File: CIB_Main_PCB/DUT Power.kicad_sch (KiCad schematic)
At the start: 27 parts, among them K18 PC357, K19 PC357, U1 HMSR_30-SMS, U2 HMSR_30-SMS

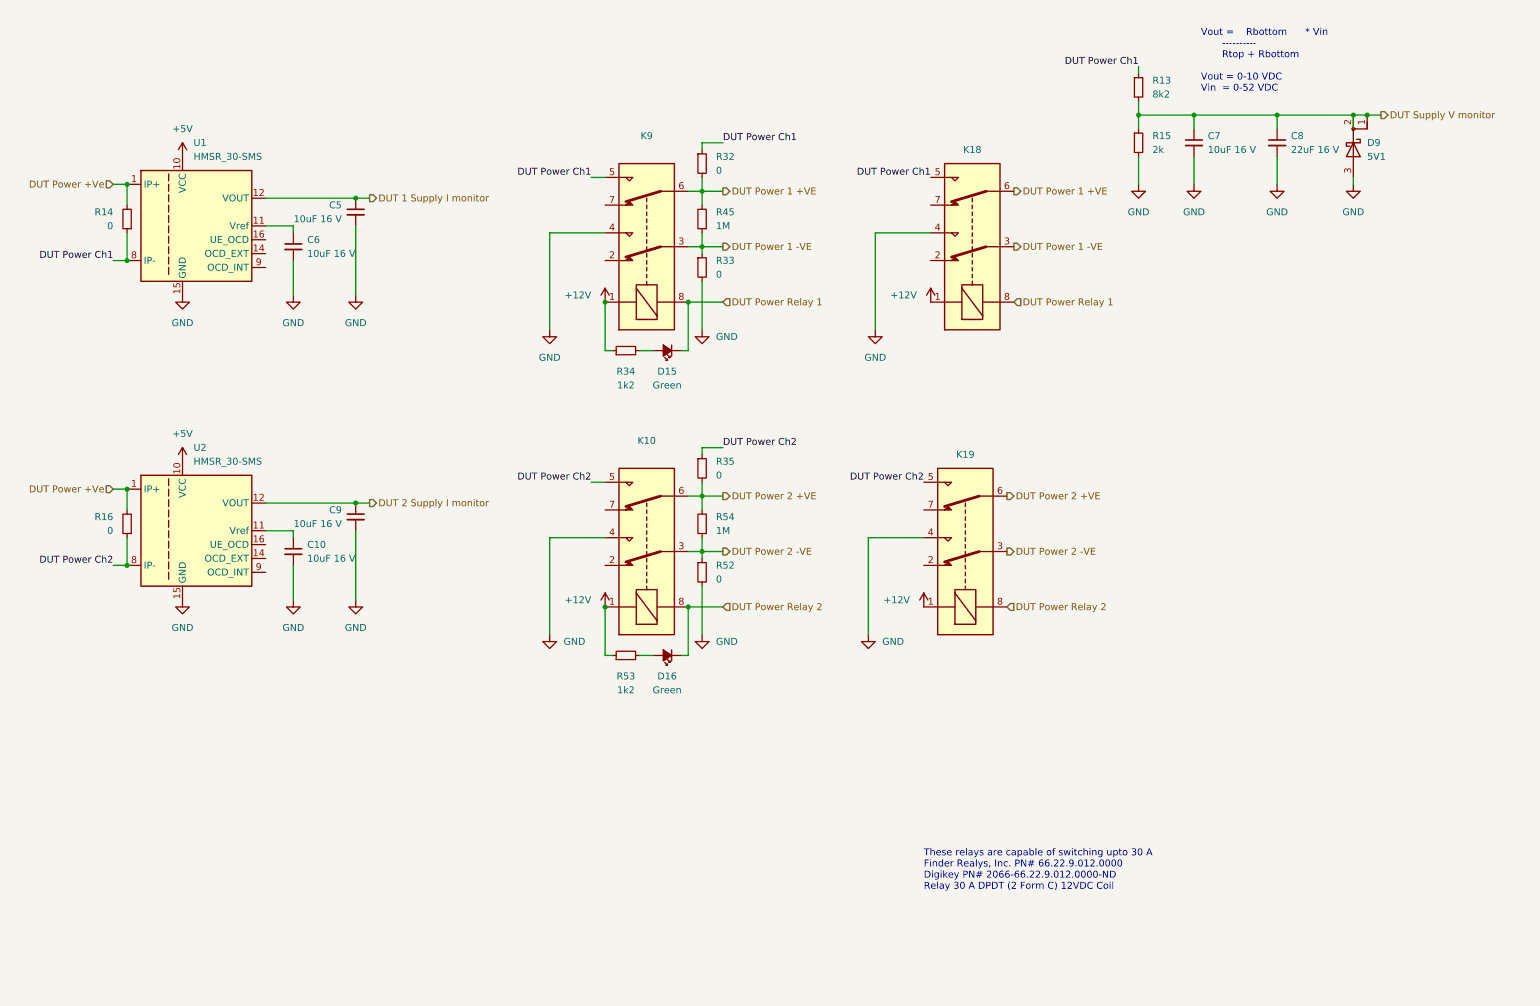
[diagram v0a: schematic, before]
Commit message: added snubbing to the relays
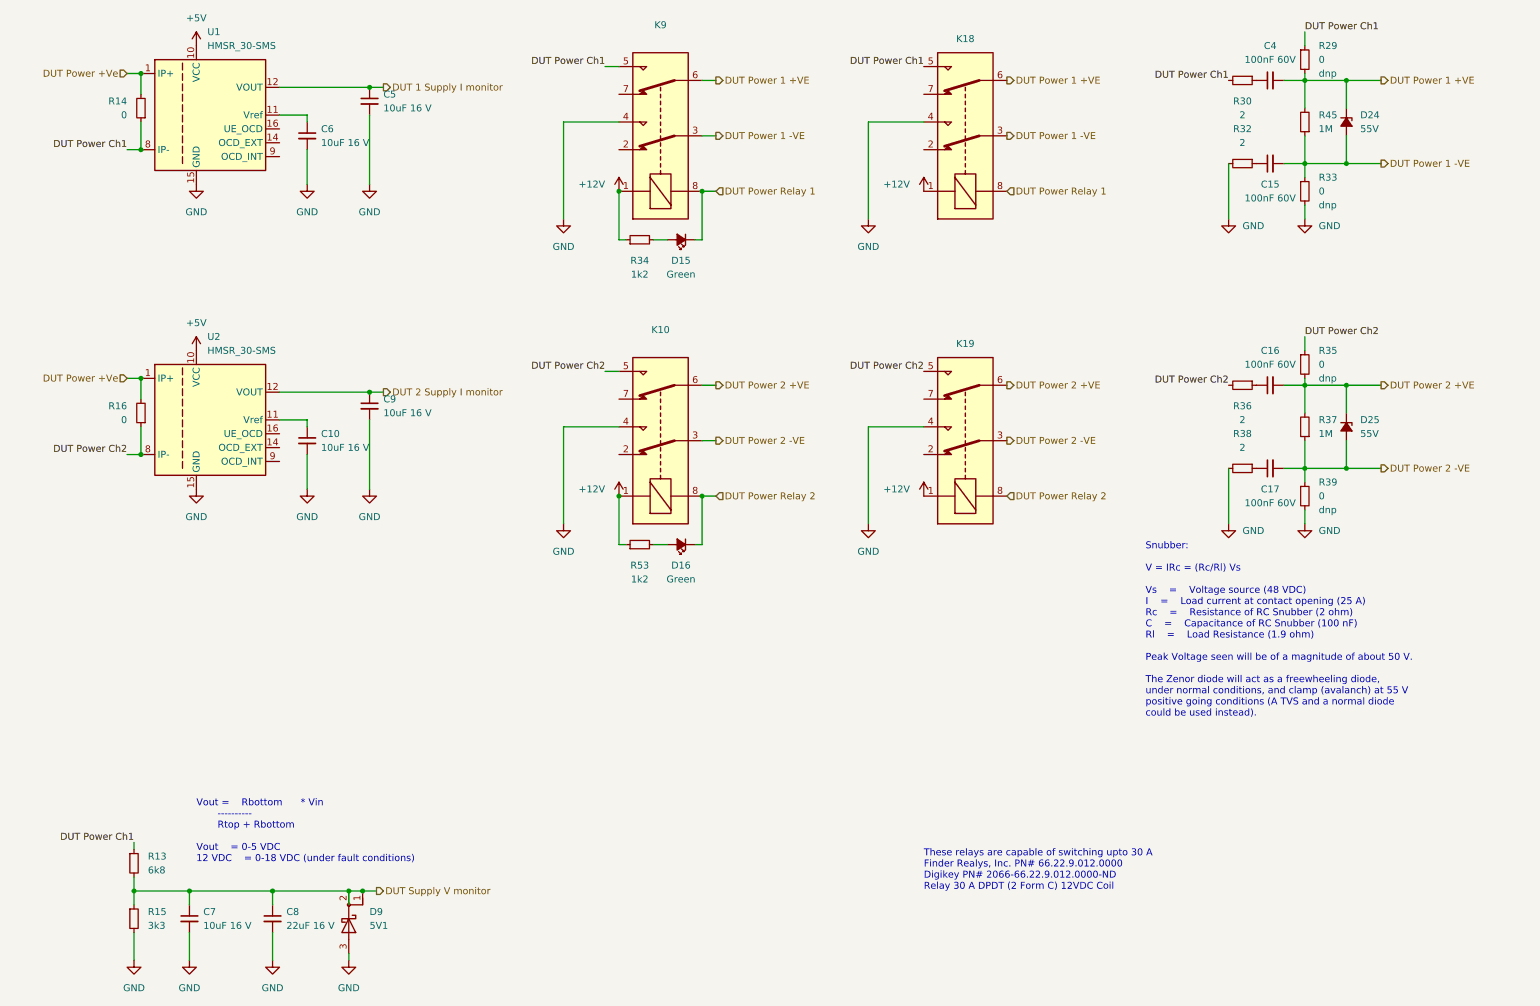
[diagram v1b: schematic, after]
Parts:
- removed R52: 0, Resistor_SMD:R_2010_5025Metric_Pad1.40x2.65mm_HandSolder, symbol Device:R_Small
- removed R54: 1M, Resistor_SMD:R_2010_5025Metric_Pad1.40x2.65mm_HandSolder, symbol Device:R_Small
- added C15, C16, C17, C4: 100nF 60V, Capacitor_SMD:C_1206_3216Metric_Pad1.33x1.80mm_HandSolder, symbol Device:C_Small
- added D24: 55V, symbol Device:D_Zener_Small_Filled
- added D25: 55V, Diode_SMD:D_SMB_Handsoldering, symbol Device:D_Zener_Small_Filled
- added R29, R39: 0, Resistor_SMD:R_2010_5025Metric_Pad1.40x2.65mm_HandSolder, symbol Device:R_Small
- added R30, R36, R38: 2, Resistor_SMD:R_2010_5025Metric_Pad1.40x2.65mm_HandSolder, symbol Device:R_Small
- added R37: 1M, Resistor_SMD:R_2010_5025Metric_Pad1.40x2.65mm_HandSolder, symbol Device:R_Small
- R13: value 8k2 -> 6k8
- R15: value 2k -> 3k3
- R32: value 0 -> 2
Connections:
- net DUT Power 1 +VE: now also C4.2, D24.1 (K), R29.2; no longer R32.2
- net DUT Power 1 -VE: now also C15.2, D24.2 (A)
- net DUT Power 2 +VE: now also C16.2, D25.1 (K), R37.2
- net DUT Power 2 -VE: now also C17.2, D25.2 (A), R37.1, R39.1
- net DUT Power Ch1: now also R29.1, R30.2; no longer R32.1
- net DUT Power Ch2: now also R36.2
- net GND: now also R32.2, R38.2, R39.2
- new net: C15.1, R32.1
- new net: C16.1, R36.1
- new net: C4.1, R30.1
- new net: C17.1, R38.1
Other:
- note added: "Snubber: V = IRc = (Rc/Rl) Vs Vs = Voltage source (48 VDC) I = Load current at contact opening (25 A) Rc = Resistance of RC Snubber (2 ohm) C = Capacitance of RC Snubber (100 nF) Rl = Load Resistance (1.9 ohm) Peak Voltage seen will be of a magnitude of about 50 V. The Zenor diode will act as a freewheeling diode, under normal conditions, and clamp (avalanch) at 55 V positive going conditions (A 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"
- note added: "Vout = Rbottom * Vin ---------- Rtop + Rbottom Vout = 0-5 VDC 12 VDC = 0-18 VDC (under fault conditions)"
- note removed: "Vout = Rbottom * Vin ---------- Rtop + Rbottom Vout = 0-10 VDC Vin = 0-52 VDC"
- moved on the sheet: C10, C5, C6, C7, C8, C9, D15, D16, D9, K10, K18, K19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
